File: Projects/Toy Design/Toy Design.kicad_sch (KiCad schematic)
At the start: 68 parts, among them J1 Conn_01x01_Pin, J2 Conn_01x01_Pin, U1 TLV61048DBVR, U2 MCP73123, U3 NCP1117-5.0_SOT223, U4 MLX90333, U5 A1330, U6 A1330, U7 LMC6484, U8 LMC6484, U9 LMC6484

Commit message: addedd mcu
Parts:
- removed R10, R11, R12, R13, R14, R15, R16, R17, R18, R19, R20, R21, R22, R23, R24, R25, R26, R27, R28, R29, R30, R31, R32, R33, R34, R35, R36, R37, R38, R39, R40, R41, R42, R7, R8, R9: R_US, Resistor_THT:R_Axial_DIN0207_L6.3mm_D2.5mm_P10.16mm_Horizontal, symbol Toy_Design:R_US
- removed U7, U8, U9: LMC6484, Package_SO:SOIC-14_3.9x8.7mm_P1.27mm, symbol Amplifier_Operational:LMC6484
- added C10, C8: 10uF, Capacitor_SMD:C_1206_3216Metric_Pad1.33x1.80mm_HandSolder, symbol Device:C
- added U10: STM32G030K6Tx, Package_QFP:LQFP-32_7x7mm_P0.8mm, symbol MCU_ST_STM32G0:STM32G030K6Tx
- added U11: MCP3208, Package_SO:SOIC-16_3.9x9.9mm_P1.27mm, symbol Analog_ADC:MCP3208
- added U7: NCP1117-3.3_SOT223, Package_TO_SOT_SMD:SOT-223-3_TabPin2, symbol Regulator_Linear:NCP1117-3.3_SOT223
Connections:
- net +5.6V: now also C8.1
- net +5V: now also C10.1, U7.2 (VO), U7.3 (VI)
- net GND: now also C10.2, C8.2, U7.1 (GND)
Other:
- moved on the sheet: C2

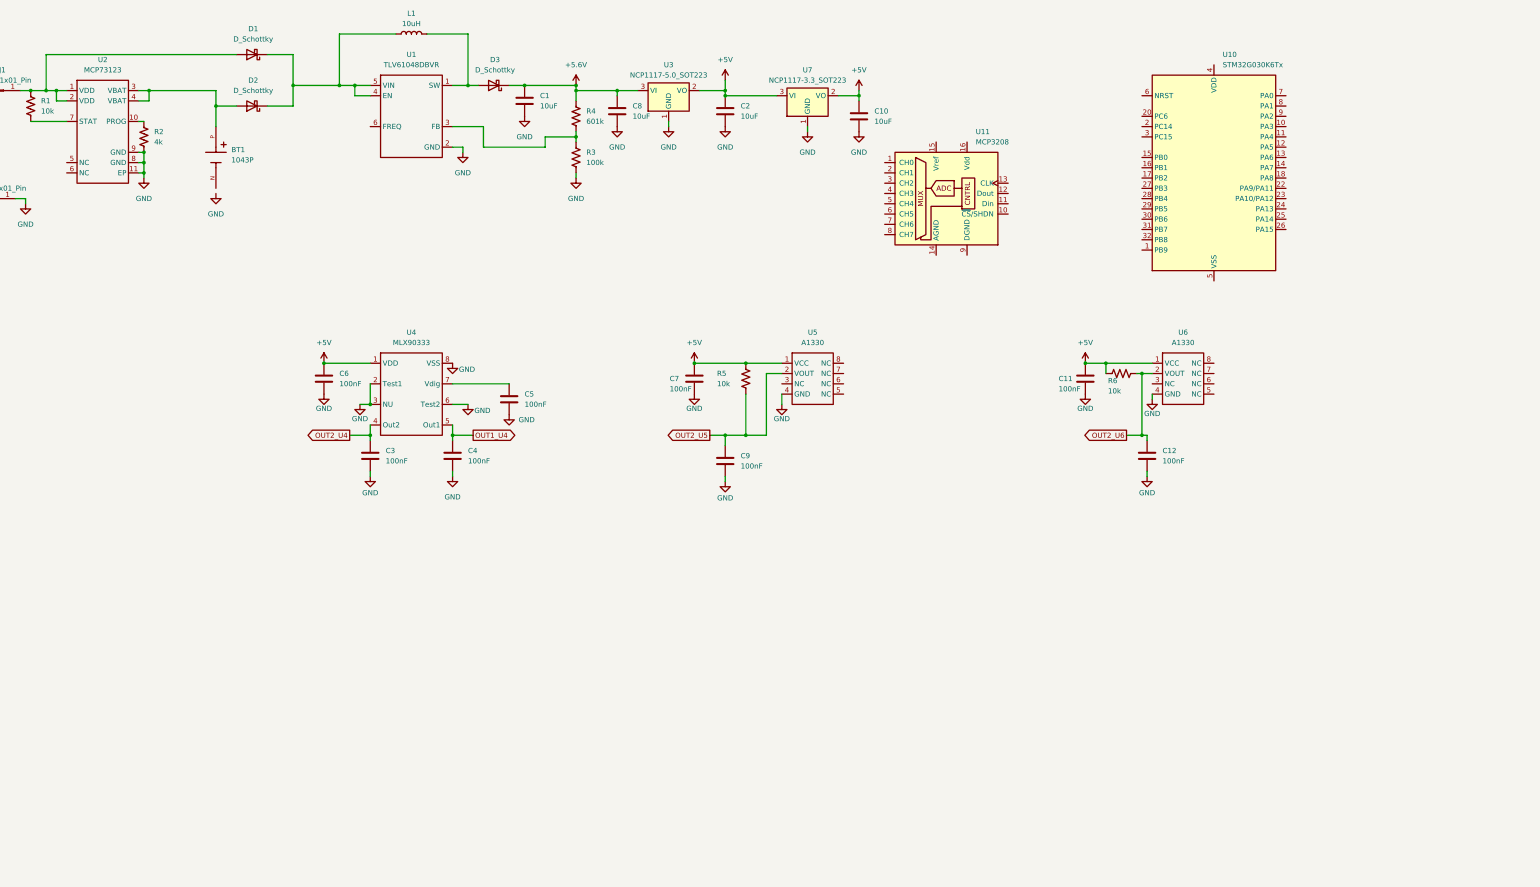
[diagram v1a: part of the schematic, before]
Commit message: Updates
Began PCB Layout and added LED controls and 3.3 to 5V level shifter
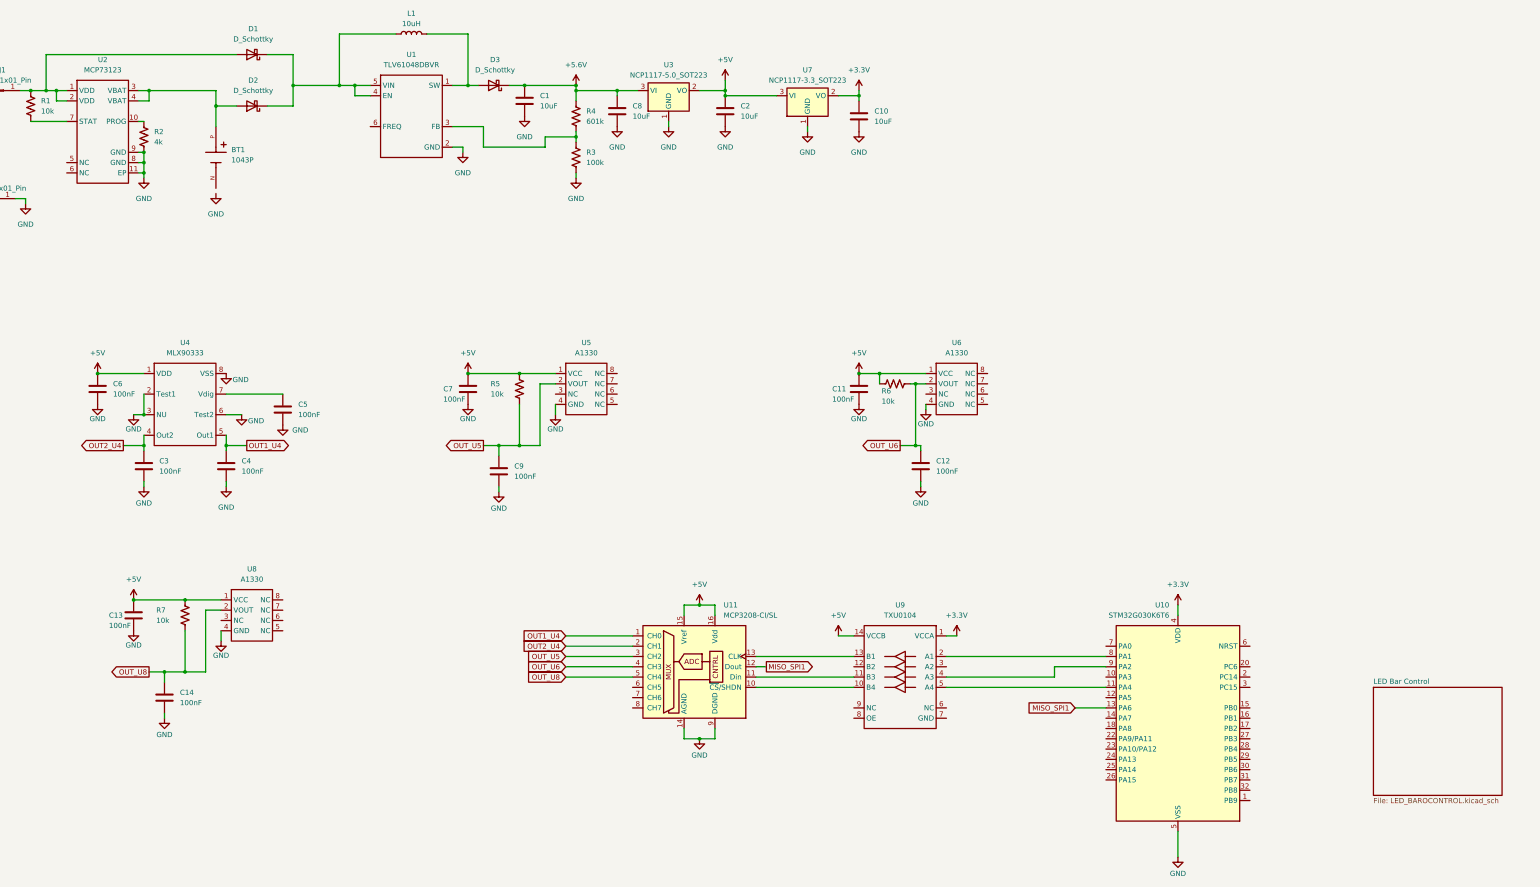
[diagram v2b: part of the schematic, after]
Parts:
- added C13, C14: 100nF, Capacitor_SMD:C_0805_2012Metric_Pad1.18x1.45mm_HandSolder, symbol Toy_Design:C
- added R7: 10k, Resistor_SMD:R_0805_2012Metric_Pad1.20x1.40mm_HandSolder, symbol Device:R_US
- added U8: A1330, Package_SO:TSSOP-8_4.4x3mm_P0.65mm, symbol Toy_Design:A1330LLETR-T
- added U9: TXU0104, Package_SO:TSSOP-14_4.4x5mm_P0.65mm, symbol Toy_Design:TXU0104
- U10: value STM32G030K6Tx -> STM32G030K6T6
- U11: value MCP3208 -> MCP3208-CI/SL
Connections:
- net OUT2_U5 is gone; now on net OUT_U5: C9.1, R5.2, U5.2 (VOUT)
- net OUT2_U6 is gone; now on net OUT_U6: C12.1, R6.2, U6.2 (VOUT)
- net +5V: now also U11.15 (Vref), U11.16 (Vdd), C13.1, R7.1, U8.1 (VCC), U9.14 (VCCB); no longer C10.1, U7.2 (VO)
- net GND: now also U10.5 (VSS), U11.14 (AGND), U11.9 (DGND), C13.2, C14.2, U8.4 (GND)
- net OUT1_U4: now also U11.1 (CH0)
- net OUT2_U4: now also U11.2 (CH1)
- net at U11.10 (~{CS}/SHDN): now also U9.10 (B4)
- net at U11.11 (Din): now also U9.11 (B3)
- net MISO_SPI1: now reaches U11.12 (Dout)
- net MISO_SPI1: now also U10.13 (PA6)
- net at U11.13 (CLK): now also U9.13 (B1)
- net OUT_U5: now reaches U11.3 (CH2)
- net OUT_U6: now reaches U11.4 (CH3)
- net OUT_U8: now reaches U11.5 (CH4)
- net OUT_U8: now also C14.1, R7.2, U8.2 (VOUT)
- net at U10.11 (PA4): now also U9.5 (A4)
- net +3.3V: now reaches U10.4 (VDD)
- net +3.3V: now also C10.1, U7.2 (VO), U9.1 (VCCA)
- net at U10.8 (PA1): now also U9.2 (A1)
- net at U10.9 (PA2): now also U9.4 (A3)
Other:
- added sheet LED Bar Control (LED_BAROCONTROL.kicad_sch)
- moved on the sheet: C11, C12, C3, C4, C5, C6, C7, C9, R5, R6, U10, U11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
